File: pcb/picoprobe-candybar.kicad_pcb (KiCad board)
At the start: 2 copper layers, 27.9 x 101.5 mm, 49 parts, among them J0 SWD-UART_PicoprobeCandybar, J1 PinHeader_2x04, J2 PinSocket_1x03, J3 PinSocket_1x02, J4 PinSocket_1x03, J5 PinSocket_1x03, J6 PinSocket_1x03, J7 PinSocket_1x02, Q1 T2N7002AK, Q2 DMP31D1U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

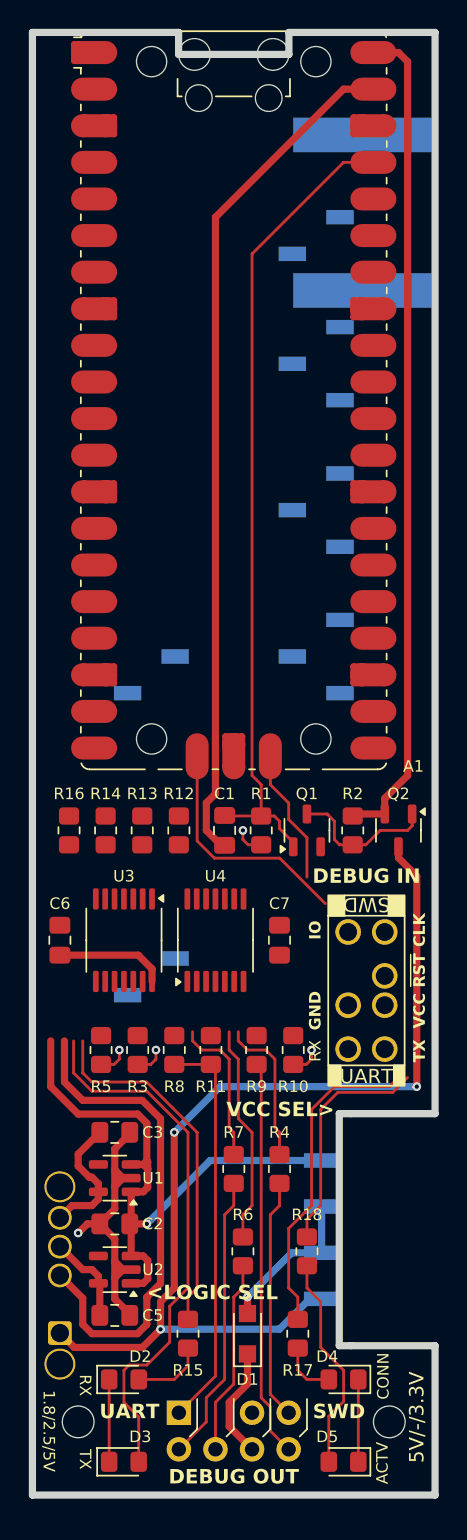
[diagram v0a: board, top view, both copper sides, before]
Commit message: Rewire debug lines 1
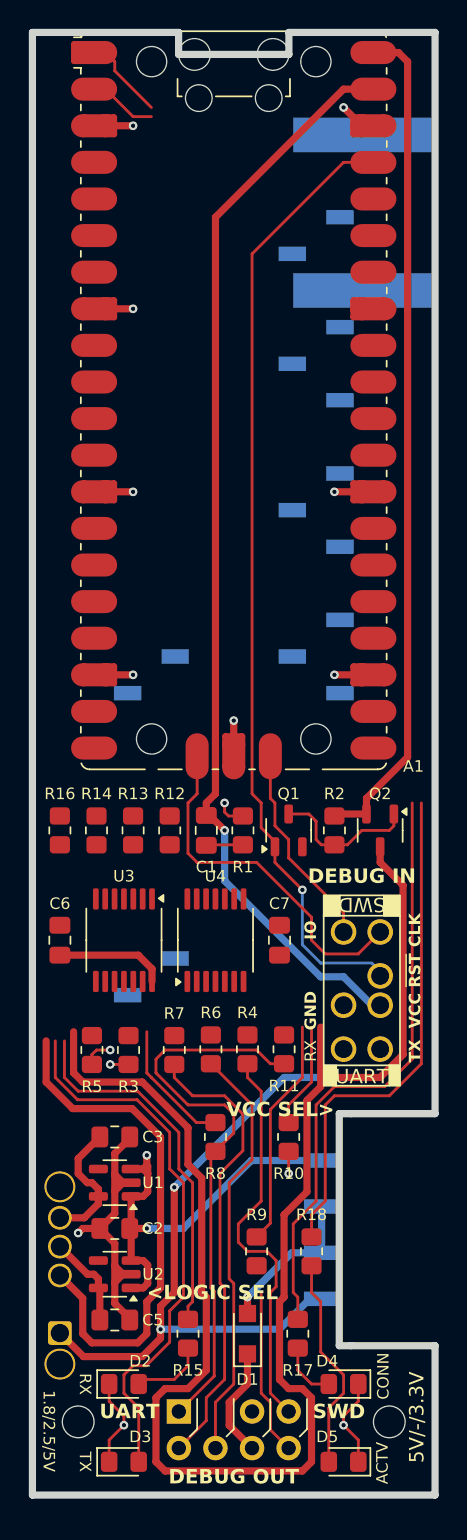
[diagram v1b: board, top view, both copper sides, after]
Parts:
- moved R6 14.2 mm to (100.0, 130.8)
- moved R9 14.0 mm to (103.2, 144.8)
- moved R7 9.23 mm to (97.5, 130.8)
- moved R4 8.59 mm to (102.6, 130.8)
- moved R8 6.68 mm to (100.3, 136.8)
- moved R10 6.04 mm to (105.4, 136.8)
- moved R11 5.08 mm to (105.1, 130.8)
- moved C1 1.27 mm to (99.7, 115.6), turned to -90 degrees
- moved Q1 1.27 mm to (105.4, 115.6)
- moved R2 1.27 mm to (108.6, 115.6)
- moved Q2 1.27 mm to (111.8, 115.6)
- moved R1 1.27 mm to (102.2, 115.6), turned to -90 degrees
- moved R12 0.64 mm to (97.2, 115.6)
- moved R13 0.64 mm to (94.6, 115.6)
- moved R16 0.64 mm to (89.5, 115.6)
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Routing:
- net GND: track 31.4 -> 129.8 mm, vias 1 -> 11
- net /GPIO16: track 16.2 -> 35.5 mm
- net /GPIO15: track 22.4 -> 41.4 mm
- net VSYS: track 58.4 -> 75.2 mm, vias 0 -> 1
- net /CB_RX: track 27.6 -> 11.6 mm
- net Net-(U4-1A): track 0.00 -> 15.9 mm
- net /CB_~{RST}: track 13.5 -> 29.2 mm
- net Net-(U3-4Y): track 15.2 -> 0.00 mm
- net /3V3_EN: track 55.9 -> 68.8 mm, vias 0 -> 1
- net 3V3: track 41.8 -> 29.1 mm, vias 1 -> 2
- net /CB_CLK: track 20.0 -> 32.0 mm
- net /CB_IO: track 27.9 -> 39.5 mm
- net /CB_TX: track 16.7 -> 27.8 mm
- net Net-(U3-2Y): track 10.5 -> 0.00 mm
- net Net-(U3-5Y): track 10.5 -> 0.00 mm
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
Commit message: Incremental Rewire debug lines 2
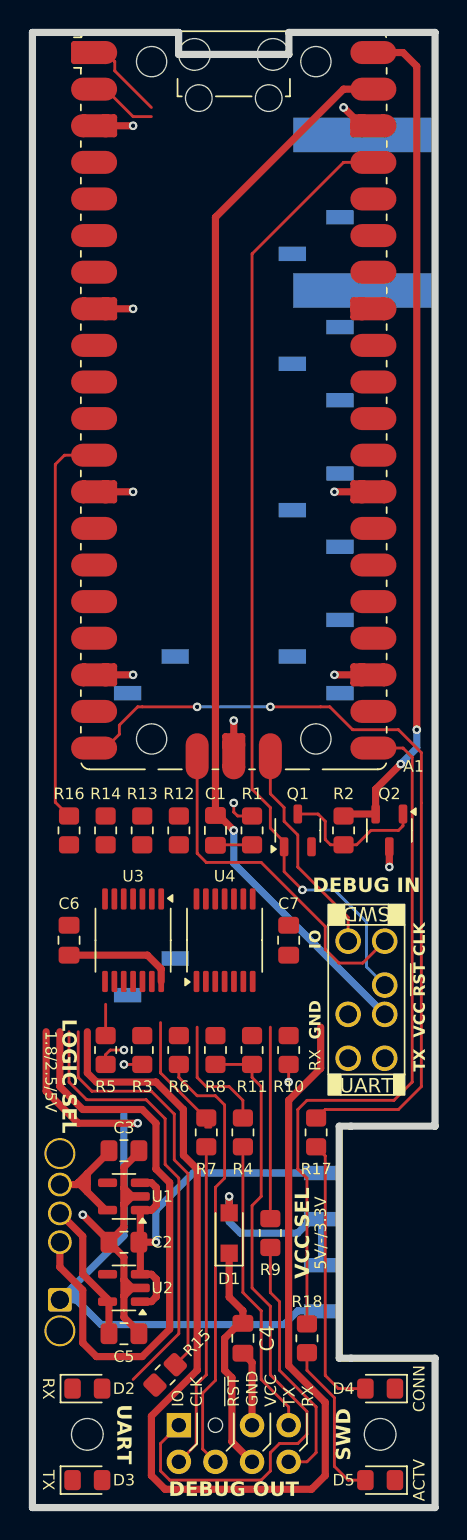
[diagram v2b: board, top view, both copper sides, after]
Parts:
- added C4: 1u, Capacitor_SMD:C_0805_2012Metric_Pad1.18x1.45mm_HandSolder, F.Cu at (102.2, 150.8)
- moved R17 14.0 mm to (107.3, 136.5)
- moved D1 7.10 mm to (101.3, 143.5)
- moved R7 6.13 mm to (99.7, 136.5)
- moved R18 6.04 mm to (106.7, 150.8)
- moved R10 6.03 mm to (105.4, 130.8)
- moved R8 6.03 mm to (100.3, 130.8)
- moved R4 5.77 mm to (102.2, 136.5)
- moved R15 3.27 mm to (96.8, 153.4), turned to -135 degrees
- moved D3 2.84 mm to (91.4, 160.7)
- moved D5 2.84 mm to (111.8, 160.7)
- moved D2 2.56 mm to (91.4, 154.3)
- moved D4 2.56 mm to (111.8, 154.3)
- moved SW3 2.31 mm to (89.5, 148.1)
- moved R11 2.22 mm to (102.9, 130.8)
- moved R6 2.22 mm to (97.8, 130.8)
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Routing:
- net /GPIO9: track 0.00 -> 28.6 mm
- net 5V: track 65.9 -> 37.6 mm, vias 3 -> 1
- net Net-(D4-A): track 4.08 -> 19.3 mm
- net /GPIO15: track 41.4 -> 56.2 mm, vias 0 -> 2
- net /GPIO16: track 35.5 -> 50.2 mm
- net /CB_CLK: track 32.0 -> 22.0 mm
- net Net-(U3-6Y): track 9.05 -> 0.00 mm
- net VOUT: track 7.72 -> 16.3 mm
- net Net-(U3-2Y): track 0.00 -> 8.55 mm
- net Net-(U3-5Y): track 0.00 -> 8.28 mm
- net /CB_TX: track 27.8 -> 20.0 mm
- net Net-(U4-2A): track 7.30 -> 0.00 mm
- net /CB_IO: track 39.5 -> 46.5 mm
- net Net-(D3-A): track 38.0 -> 31.0 mm
- net GND: track 129.8 -> 136.1 mm, vias 11 -> 10
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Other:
- board size 27.9 x 101.5 mm -> 27.9 x 102.4 mm
- board text added: "IO CLK ~{RST} GND VCC TX RX"
- board text added: "LOGIC SEL"
- board text added: "VCC SEL"
- board text removed: "<LOGIC SEL"
- board text removed: "VCC SEL>"

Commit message: Update components in draft layout
Layout still heavily in-progress
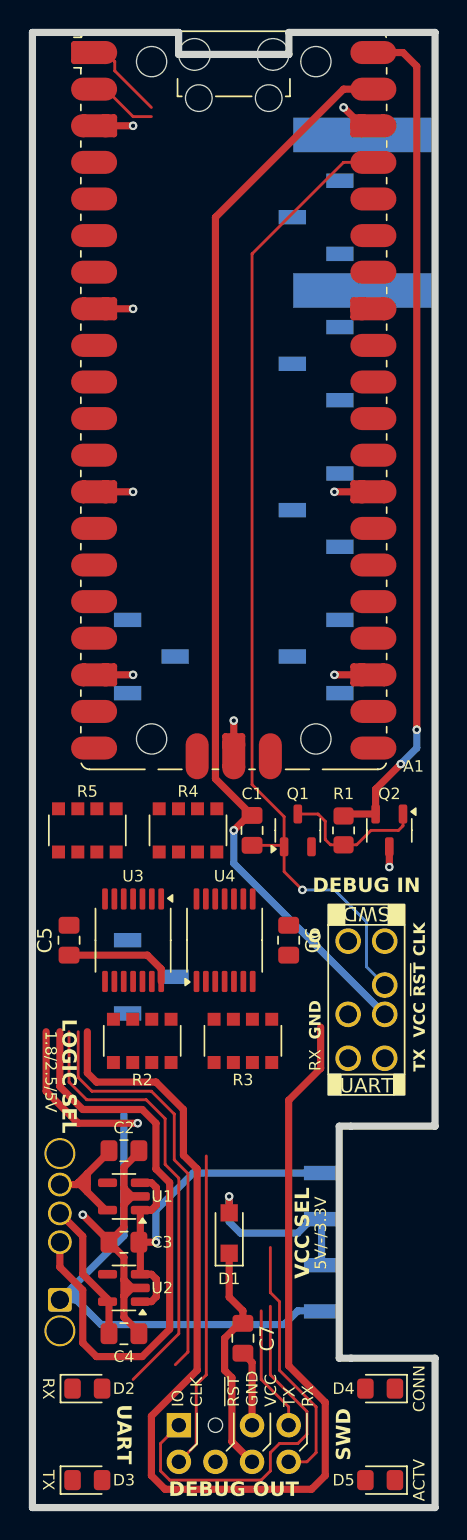
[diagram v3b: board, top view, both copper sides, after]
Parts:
- removed the C7 at (105.4, 123.2)
- removed the R1 at (102.9, 115.6)
- removed R10, R11, R12, R13, R14, R6, R7, R8, R9: 100R, Resistor_SMD:R_0805_2012Metric_Pad1.20x1.40mm_HandSolder
- removed R15, R16, R17, R18: 470R, Resistor_SMD:R_0805_2012Metric_Pad1.20x1.40mm_HandSolder
- removed REF** (x2): MountingHole_2.2mm_M2_ISO7380, MountingHole:MountingHole_2.2mm_M2_ISO7380
- added C5: 1u, Capacitor_SMD:C_0805_2012Metric_Pad1.18x1.45mm_HandSolder, F.Cu at (90.2, 123.2)
- added R2: 100R, Resistor_SMD:R_Array_Convex_4x1206, F.Cu at (95.2, 130.2)
- J2: footprint Connector_PinSocket_2.54mm:PinSocket_1x02_P2.54mm_Vertical_SMD_Pin1Left -> Connector_PinSocket_2.54mm:PinSocket_1x03_P2.54mm_Vertical_SMD_Pin1Left
- J3, J7: value PinSocket_1x02 -> PinSocket_1x03; footprint Connector_PinSocket_2.54mm:PinSocket_1x02_P2.54mm_Vertical_SMD_Pin1Left -> Connector_PinSocket_2.54mm:PinSocket_1x03_P2.54mm_Vertical_SMD_Pin1Left
- R3, R4: footprint Resistor_SMD:R_0805_2012Metric_Pad1.20x1.40mm_HandSolder -> Resistor_SMD:R_Array_Convex_4x1206
- R5: value 100R -> 470R; footprint Resistor_SMD:R_0805_2012Metric_Pad1.20x1.40mm_HandSolder -> Resistor_SMD:R_Array_Convex_4x1206
- moved R4 21.3 mm to (98.4, 115.6), turned to 90 degrees
- moved R5 15.3 mm to (91.4, 115.6)
- moved C6 15.2 mm to (105.4, 123.2), turned to -90 degrees
- moved R3 7.01 mm to (102.2, 130.2)
- moved C1 2.54 mm to (102.9, 115.6)
- moved J3 1.27 mm to (95.9, 103.5)
- moved J7 1.27 mm to (107.3, 73.0)
- renumbered C3 to C2, C2 to C3, C5 to C4, C4 to C7, R2 to R1
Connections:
- net /GPIO12 renamed /CLK
- net /GPIO13 renamed /IO_OUT
- net /GPIO14 renamed /IO_IN
- net /GPIO17 renamed /RS1
- net /GPIO18 renamed /RS2
- net /GPIO19 renamed /RS3
- net /GPIO20 renamed /CB_RS4
- net /GPIO21 renamed /CB_RS5
- net /GPIO22 renamed /CB_RS6
- net /GPIO3 renamed /DTR
- net /GPIO4 renamed /TX
- net /GPIO5 renamed /RX
- net /GPIO6 renamed /CTS
- net /GPIO7 renamed /RTS
- A1 pad 11: /GPIO8 -> /LED_TX
- A1 pad 12: /GPIO9 -> /LED_RX
- A1 pad 20: /GPIO15 -> /LED_CON
- A1 pad 21: /GPIO16 -> /LED_RUN
- A1 pad 4: /GPIO2 -> /CB_~{RST}
- C6 pad 1: VLOGIC -> 3V3
- J4 pad 1: /RSV_3 -> /CB_RS3
- J4 pad 2: /RSV_2 -> /CB_RS2
- J4 pad 3: /RSV_1 -> /CB_RS1
- R3 pad 1: Net-(U3-1Y) -> Net-(R3A-R1.1)
- R3 pad 2: /CB_DTR -> Net-(R3B-R2.1)
- R4 pad 1: Net-(U3-2Y) -> Net-(R4A-R1.1)
- R4 pad 2: /CB_TX -> Net-(R4B-R2.1)
- R5 pad 1: Net-(U3-3Y) -> /LED_TX
- R5 pad 2: /CB_RTS -> /LED_RX
- U3 pad 10: Net-(U3-5Y) -> Net-(R3A-R1.1)
- U3 pad 12: Net-(U3-6Y) -> Net-(R3B-R2.1)
- U3 pad 2: Net-(U3-1Y) -> Net-(R2B-R2.1)
- U3 pad 4: Net-(U3-2Y) -> Net-(R2C-R3.1)
- U3 pad 6: Net-(U3-3Y) -> Net-(R2D-R4.1)
- U3 pad 8: Net-(U3-4Y) -> unconnected-(U3-4Y-Pad8)
- U3 pad 9: /GPIO2 -> unconnected-(U3-4A-Pad9)
- U4 pad 1: Net-(U4-1A) -> Net-(R3C-R3.1)
- U4 pad 11: Net-(U4-5A) -> Net-(R4C-R3.1)
- U4 pad 13: Net-(U4-6A) -> Net-(R4D-R4.1)
- U4 pad 3: Net-(U4-2A) -> Net-(R3D-R4.1)
- U4 pad 5: Net-(U4-3A) -> Net-(R4A-R1.1)
- U4 pad 9: Net-(U4-4A) -> Net-(R4B-R2.1)
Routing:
- net /GPIO15: track 56.2 -> 0.00 mm, vias 2 -> 0
- net /GPIO16: track 50.2 -> 0.00 mm
- net /CB_~{RST}: track 30.6 -> 0.00 mm
- net /GPIO8: track 29.0 -> 0.00 mm
- net (no net): track 0.00 -> 29.0 mm
- net /GPIO9: track 28.6 -> 0.00 mm
- net Net-(A1-SWCLK): track 25.3 -> 0.00 mm
- net /CB_IO: track 46.5 -> 26.1 mm
- net Net-(D4-A): track 19.3 -> 0.00 mm
- net Net-(A1-SWDIO): track 16.7 -> 0.86 mm
- net Net-(U4-1A): track 12.7 -> 0.00 mm
- net /CB_TX: track 20.0 -> 8.73 mm
- net Net-(D5-A): track 11.2 -> 0.00 mm
- net Net-(U3-2Y): track 8.55 -> 0.00 mm
- net Net-(U3-5Y): track 8.28 -> 0.00 mm
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
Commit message: Major in-progress layout redesign
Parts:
- A1: footprint Module_RaspberryPi_Pico:RaspberryPi_Pico_Original_SMD_MountingHoles_HandSolder -> Module_RaspberryPi_Pico:RaspberryPi_Pico_Original_SMD_HandSolder
- moved R5 34.1 mm to (105.4, 146.7)
- moved R4 25.5 mm to (100.3, 141.0), turned to -90 degrees
- moved Q2 17.8 mm to (112.1, 133.3), turned to 180 degrees
- moved J0 16.3 mm to (93.3, 125.1), turned to 180 degrees
- moved R1 14.9 mm to (112.1, 130.2), turned to 0 degrees
- moved J2 14.6 mm to (95.9, 111.1)
- moved C5 13.6 mm to (103.5, 120.7)
- moved Q1 12.9 mm to (112.1, 127.0), turned to 0 degrees
- moved C1 12.4 mm to (112.1, 123.8), turned to 180 degrees
- moved U4 9.69 mm to (109.2, 118.1)
- moved C6 7.62 mm to (105.4, 115.6)
- moved U3 7.18 mm to (99.7, 118.1)
- moved R2 4.84 mm to (99.7, 128.3)
- moved R3 4.26 mm to (106.0, 128.3)
- moved D1 3.55 mm to (99.7, 146.7)
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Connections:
- A1 pad 4: /CB_~{RST} -> /~{RST}
- J2 pad 2: /CB_CTS -> /CB_RTS
- J2 pad 3: /CB_RTS -> /CB_CTS
- J3 pad 1: /INT_RISE -> unconnected-(J3-Pin_1-Pad1)
- J3 pad 3: unconnected-(J3-Pin_3-Pad3) -> /INT_RISE
- R2 pad 1: Net-(R2A-R1.1) -> /CB_RS1
- R2 pad 2: Net-(R2B-R2.1) -> /CB_CTS
- R2 pad 3: Net-(R2C-R3.1) -> /CB_RX
- R2 pad 4: Net-(R2D-R4.1) -> /3V3_EN
- R2 pad 5: /CB_RTS -> Net-(R2D-R4.2)
- R2 pad 6: /CB_TX -> Net-(R2C-R3.2)
- R2 pad 7: /CB_DTR -> Net-(R2B-R2.2)
- R2 pad 8: /3V3_EN -> Net-(R2A-R1.2)
- R3 pad 1: Net-(R3A-R1.1) -> /CB_RTS
- R3 pad 2: Net-(R3B-R2.1) -> /CB_CLK
- R3 pad 3: Net-(R3C-R3.1) -> /CB_DTR
- R3 pad 4: Net-(R3D-R4.1) -> /CB_TX
- R3 pad 5: /CB_CTS -> Net-(R3D-R4.2)
- R3 pad 6: /CB_RX -> Net-(R3C-R3.2)
- R3 pad 7: /CB_IO -> Net-(R3B-R2.2)
- R3 pad 8: /CB_CLK -> Net-(R3A-R1.2)
- R4 pad 1: Net-(R4A-R1.1) -> /~{RST}
- R4 pad 4: Net-(R4D-R4.1) -> /IO_SHIFTED
- R4 pad 5: /CB_RS3 -> /CB_IO
- R4 pad 7: /CB_RS1 -> /CB_RS3
- R4 pad 8: /CB_IO -> /CB_~{RST}
- R5 pad 1: /LED_TX -> /LED_RX
- R5 pad 2: /LED_RX -> /LED_TX
- R5 pad 7: Net-(D3-A) -> Net-(D2-A)
- R5 pad 8: Net-(D2-A) -> Net-(D3-A)
- SW1 pad 2: Net-(R2A-R1.1) -> Net-(R2D-R4.2)
- U3 pad 1: /DTR -> /RTS
- U3 pad 10: Net-(R3A-R1.1) -> Net-(R3C-R3.2)
- U3 pad 11: /CLK -> /DTR
- U3 pad 12: Net-(R3B-R2.1) -> unconnected-(U3-6Y-Pad12)
- U3 pad 13: /IO_OUT -> unconnected-(U3-6A-Pad13)
- U3 pad 2: Net-(R2B-R2.1) -> Net-(R3A-R1.2)
- U3 pad 3: /TX -> /CLK
- U3 pad 4: Net-(R2C-R3.1) -> Net-(R3B-R2.2)
- U3 pad 5: /RTS -> /IO_OUT
- U3 pad 6: Net-(R2D-R4.1) -> /IO_SHIFTED
- U3 pad 8: unconnected-(U3-4Y-Pad8) -> Net-(R3D-R4.2)
- U3 pad 9: unconnected-(U3-4A-Pad9) -> /TX
- U4 pad 1: Net-(R3C-R3.1) -> Net-(R4B-R2.1)
- U4 pad 10: /RS2 -> /CTS
- U4 pad 11: Net-(R4C-R3.1) -> Net-(R2B-R2.2)
- U4 pad 12: /RS3 -> /IO_IN
- U4 pad 13: Net-(R4D-R4.1) -> /IO_SHIFTED
- U4 pad 2: /RX -> /RS3
- U4 pad 3: Net-(R3D-R4.1) -> Net-(R4C-R3.1)
- U4 pad 4: /CTS -> /RS2
- U4 pad 5: Net-(R4A-R1.1) -> Net-(R2A-R1.2)
- U4 pad 6: /IO_IN -> /RS1
- U4 pad 8: /RS1 -> /RX
- U4 pad 9: Net-(R4B-R2.1) -> Net-(R2C-R3.2)
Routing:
- net /~{RST}: track 0.00 -> 76.5 mm
- net /DTR: track 0.00 -> 57.0 mm
- net 3V3: track 28.0 -> 82.9 mm, vias 1 -> 3
- net /TX: track 0.00 -> 53.0 mm
- net /RX: track 0.02 -> 47.5 mm, vias 0 -> 2
- net Net-(A1-GPIO0): track 5.13 -> 52.3 mm
- net Net-(A1-GPIO1): track 3.96 -> 48.6 mm
- net VLOGIC: track 48.7 -> 4.85 mm
- net /CTS: track 0.00 -> 41.9 mm, vias 0 -> 2
- net /RTS: track 0.00 -> 36.0 mm
- net /IO_SHIFTED: track 0.00 -> 35.9 mm, vias 0 -> 2
- net AGND: track 0.00 -> 34.0 mm
- net (no net): track 29.0 -> 0.00 mm
- net /RS3: track 0.00 -> 25.5 mm
- net /RS2: track 0.00 -> 23.2 mm
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
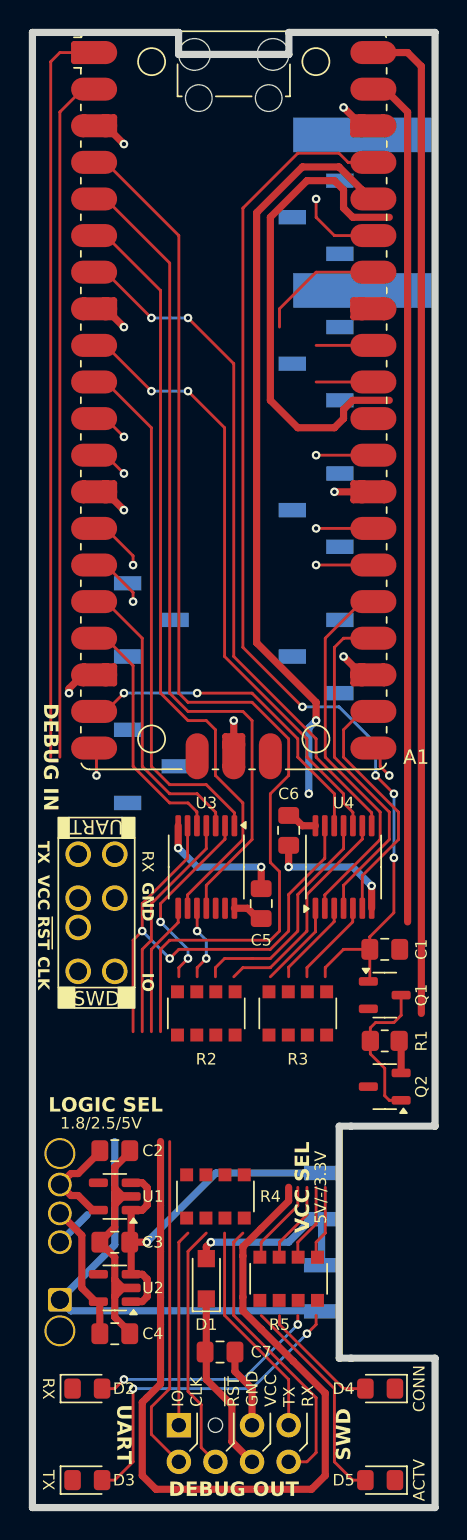
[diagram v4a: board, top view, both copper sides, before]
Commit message: Major layout refactor (sans ground planes)
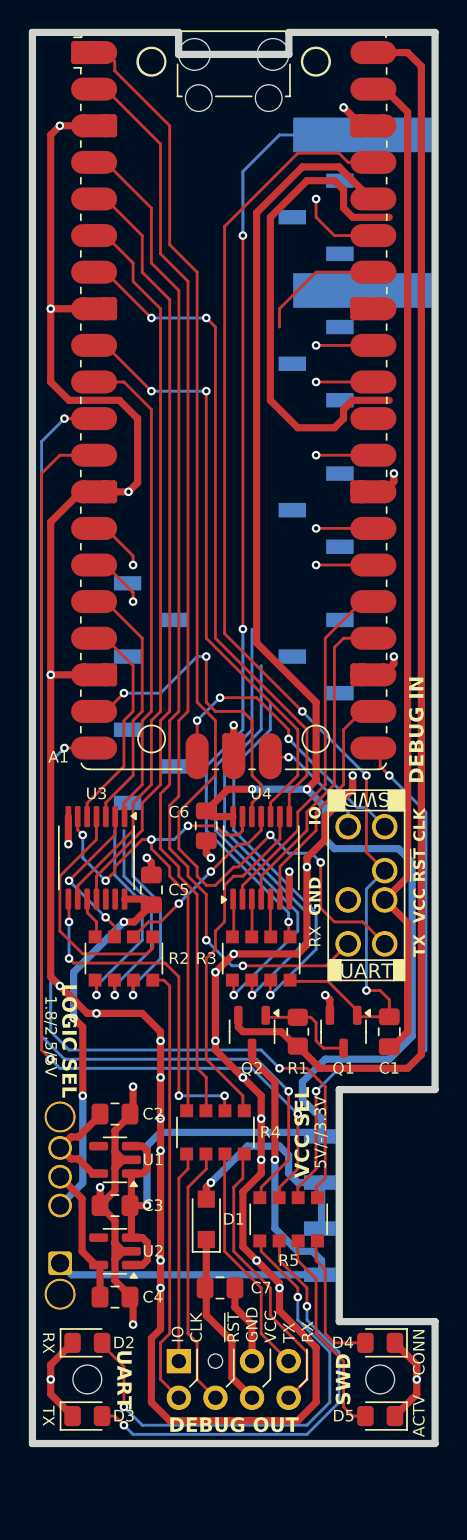
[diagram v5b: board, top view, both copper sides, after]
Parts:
- added REF**: MountingHole_2mm, MountingHole:MountingHole_2mm, F.Cu at (111.8, 153.7)
- added REF**: MountingHole_2mm, MountingHole:MountingHole_2mm, F.Cu at (107.3, 62.2)
- added REF**: MountingHole_2mm, MountingHole:MountingHole_2mm, F.Cu at (91.4, 153.7)
- added REF**: MountingHole_2mm, MountingHole:MountingHole_2mm, F.Cu at (95.9, 62.2)
- moved J0 18.8 mm to (109.5, 115.6), turned to 0 degrees
- moved Q2 9.96 mm to (102.9, 129.5), turned to -90 degrees
- moved C5 7.68 mm to (95.9, 119.7)
- moved U3 7.65 mm to (92.1, 117.5)
- moved R2 6.87 mm to (94.0, 124.5), turned to 90 degrees
- moved R1 6.07 mm to (106.0, 129.5), turned to -90 degrees
- moved U4 5.75 mm to (103.5, 117.5)
- moved C6 5.72 mm to (99.7, 115.3)
- moved C1 5.72 mm to (112.4, 129.5), turned to 90 degrees
- moved R3 4.58 mm to (103.5, 124.5), turned to 90 degrees
- moved C7 4.44 mm to (100.6, 147.3)
- moved D3 4.44 mm to (91.4, 156.2)
- moved D5 4.44 mm to (111.8, 156.2)
- moved J1 4.44 mm to (97.8, 152.4)
- moved R4 4.44 mm to (100.3, 136.5), turned to 90 degrees
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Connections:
- J2 pad 1: /CB_DTR -> /CB_CTS
- J2 pad 3: /CB_CTS -> /CB_DTR
- R2 pad 1: /CB_RS1 -> /CB_DTR
- R2 pad 2: /CB_CTS -> /CB_RTS
- R2 pad 3: /CB_RX -> /CB_CTS
- R2 pad 4: /3V3_EN -> /CB_CLK
- R3 pad 1: /CB_RTS -> /CB_RS3
- R3 pad 2: /CB_CLK -> /CB_RS2
- R3 pad 3: /CB_DTR -> /CB_RS1
- R3 pad 4: /CB_TX -> /3V3_EN
- R4 pad 1: /~{RST} -> /CB_IO
- R4 pad 2: Net-(R4B-R2.1) -> /CB_~{RST}
- R4 pad 3: Net-(R4C-R3.1) -> /CB_TX
- R4 pad 4: /IO_SHIFTED -> /CB_RX
- R4 pad 5: /CB_IO -> Net-(R4D-R4.2)
- R4 pad 6: /CB_RS2 -> Net-(R4C-R3.2)
- R4 pad 7: /CB_RS3 -> /~{RST}
- R4 pad 8: /CB_~{RST} -> /IO_SHIFTED
- R5 pad 1: /LED_RX -> Net-(D2-A)
- R5 pad 2: /LED_TX -> Net-(D3-A)
- R5 pad 3: /LED_CON -> Net-(D5-A)
- R5 pad 4: /LED_RUN -> Net-(D4-A)
- R5 pad 5: Net-(D5-A) -> /LED_CON
- R5 pad 6: Net-(D4-A) -> /LED_RUN
- R5 pad 7: Net-(D2-A) -> /LED_RX
- R5 pad 8: Net-(D3-A) -> /LED_TX
- SW1 pad 2: Net-(R2D-R4.2) -> Net-(R3D-R4.2)
- U3 pad 10: Net-(R3C-R3.2) -> Net-(R2A-R1.2)
- U3 pad 2: Net-(R3A-R1.2) -> Net-(R2B-R2.2)
- U3 pad 4: Net-(R3B-R2.2) -> Net-(R2D-R4.2)
- U3 pad 8: Net-(R3D-R4.2) -> Net-(R4C-R3.2)
- U4 pad 1: Net-(R4B-R2.1) -> Net-(R3A-R1.2)
- U4 pad 11: Net-(R2B-R2.2) -> Net-(R2C-R3.2)
- U4 pad 3: Net-(R4C-R3.1) -> Net-(R3B-R2.2)
- U4 pad 5: Net-(R2A-R1.2) -> Net-(R3C-R3.2)
- U4 pad 9: Net-(R2C-R3.2) -> Net-(R4D-R4.2)
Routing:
- net GND: track 119.2 -> 239.7 mm, vias 12 -> 36
- net /LED_TX: track 7.18 -> 73.3 mm, vias 1 -> 2
- net /LED_RX: track 6.95 -> 70.9 mm, vias 1 -> 2
- net Net-(R3D-R4.2): track 9.34 -> 65.9 mm, vias 0 -> 3
- net 3V3: track 82.9 -> 129.1 mm
- net /LED_CON: track 7.82 -> 51.6 mm, vias 1 -> 2
- net /CB_RS3: track 0.00 -> 31.7 mm, vias 0 -> 1
- net /LED_RUN: track 9.38 -> 40.3 mm, vias 1 -> 2
- net Net-(A1-GPIO0): track 52.3 -> 81.6 mm, vias 0 -> 2
- net /CB_RS2: track 0.00 -> 28.9 mm, vias 0 -> 1
- net /CB_RS1: track 0.00 -> 26.1 mm, vias 0 -> 1
- net Net-(A1-GPIO1): track 48.6 -> 74.2 mm, vias 0 -> 2
- net Net-(R4C-R3.2): track 0.00 -> 24.8 mm, vias 0 -> 4
- net Net-(R4D-R4.2): track 0.00 -> 24.0 mm
- net VLOGIC: track 4.85 -> 26.5 mm, vias 0 -> 3
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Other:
- board size 27.9 x 102.4 mm -> 27.9 x 97.9 mm
